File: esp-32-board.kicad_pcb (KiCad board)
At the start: 2 copper layers, 53.8 x 69.1 mm, 35 parts, among them J1 Conn_Arduino_UNO_R3, J2 Conn_02x03_Odd_Even, J3 ESP-PROG-Program, J4 ESP-PROG-Debug, J5 Barrel_Jack_MountingPin, J6 USB_B_Micro, Q2 ?, Q3 ?, SW1 SW_Push, SW2 SW_Push, SW3 SW_SPST, U1 ESP32-WROOM-32, U3 NCP1117-3.3, U4 NCP1117ST50T3G, U5 USBLC6-2SC6, U6 CP2102N-A01-GQFN28

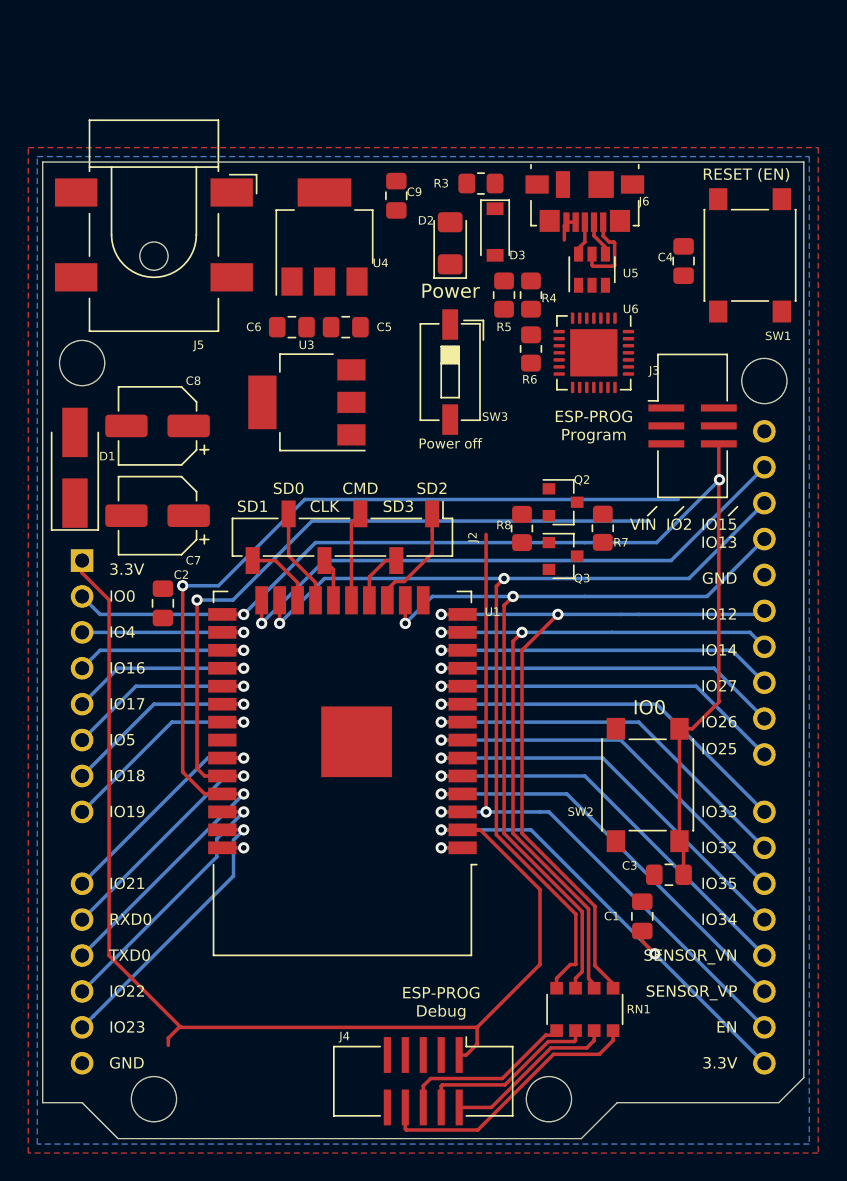
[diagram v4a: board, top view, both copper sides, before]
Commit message: Connect rest of tracks
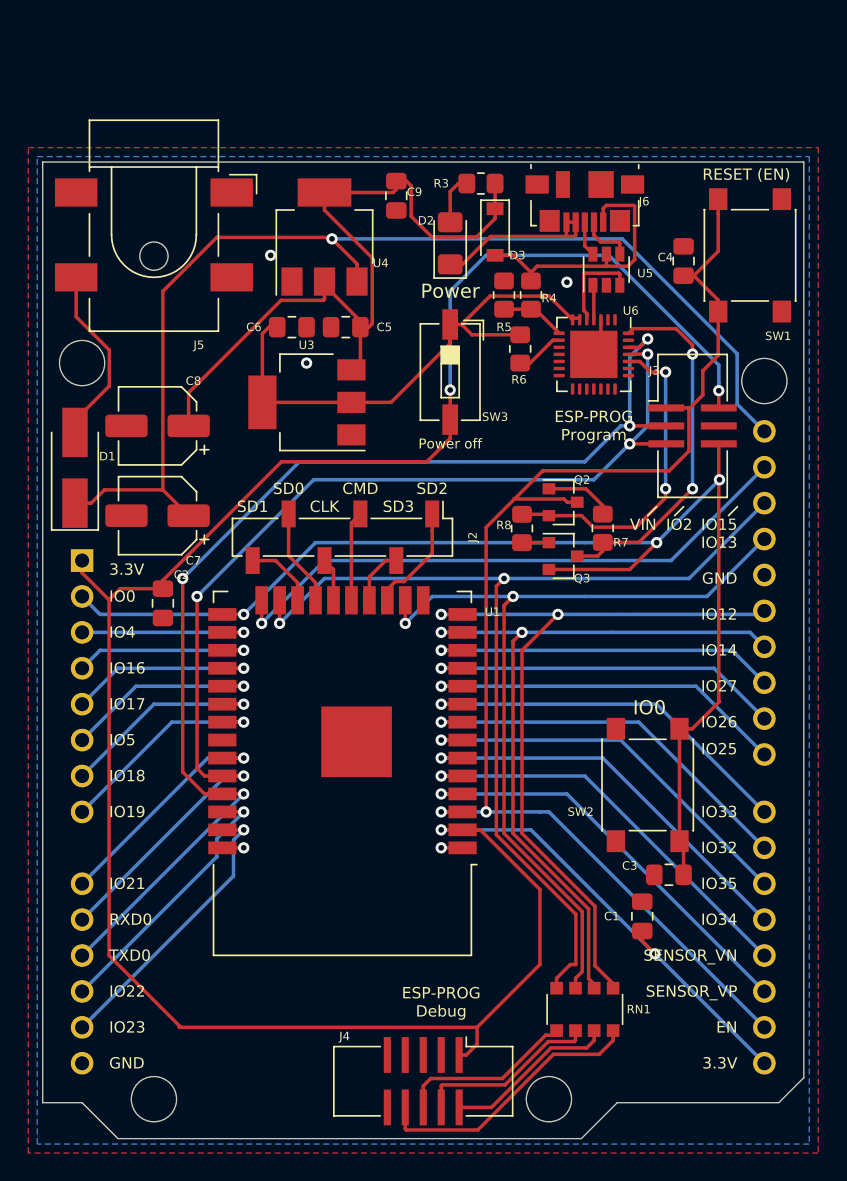
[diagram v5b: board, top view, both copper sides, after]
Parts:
- moved U5 1.02 mm to (169.2, 29.0)
- moved R6 0.76 mm to (163.1, 34.6)
- moved U6 0.11 mm to (168.3, 34.9)
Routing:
- net VDC: track 0.00 -> 78.9 mm, vias 0 -> 1
- net +3V3: track 113.4 -> 177.7 mm, vias 2 -> 4
- net +5V: track 0.00 -> 53.8 mm
- net /EN: track 50.3 -> 94.4 mm
- net /Power/Internal_3V3: track 0.00 -> 37.6 mm
- net /USB/DTR: track 0.00 -> 25.8 mm, vias 0 -> 2
- net /USB/RTS: track 0.00 -> 23.2 mm, vias 0 -> 2
- net /USB/VBUS: track 6.01 -> 19.3 mm
- net GND: track 5.18 -> 18.2 mm, vias 2 -> 5
- net Net-(D1-Pad2): track 0.00 -> 13.0 mm
- net /RXD0: track 65.4 -> 77.2 mm, vias 2 -> 4
- net /TXD0: track 71.9 -> 81.8 mm, vias 2 -> 4
- net /IO0: track 83.4 -> 91.8 mm, vias 2 -> 3
- net /USB/USB_DN: track 0.00 -> 6.71 mm
- net Net-(Q2-Pad1): track 0.00 -> 4.90 mm
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
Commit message: Update DC connector
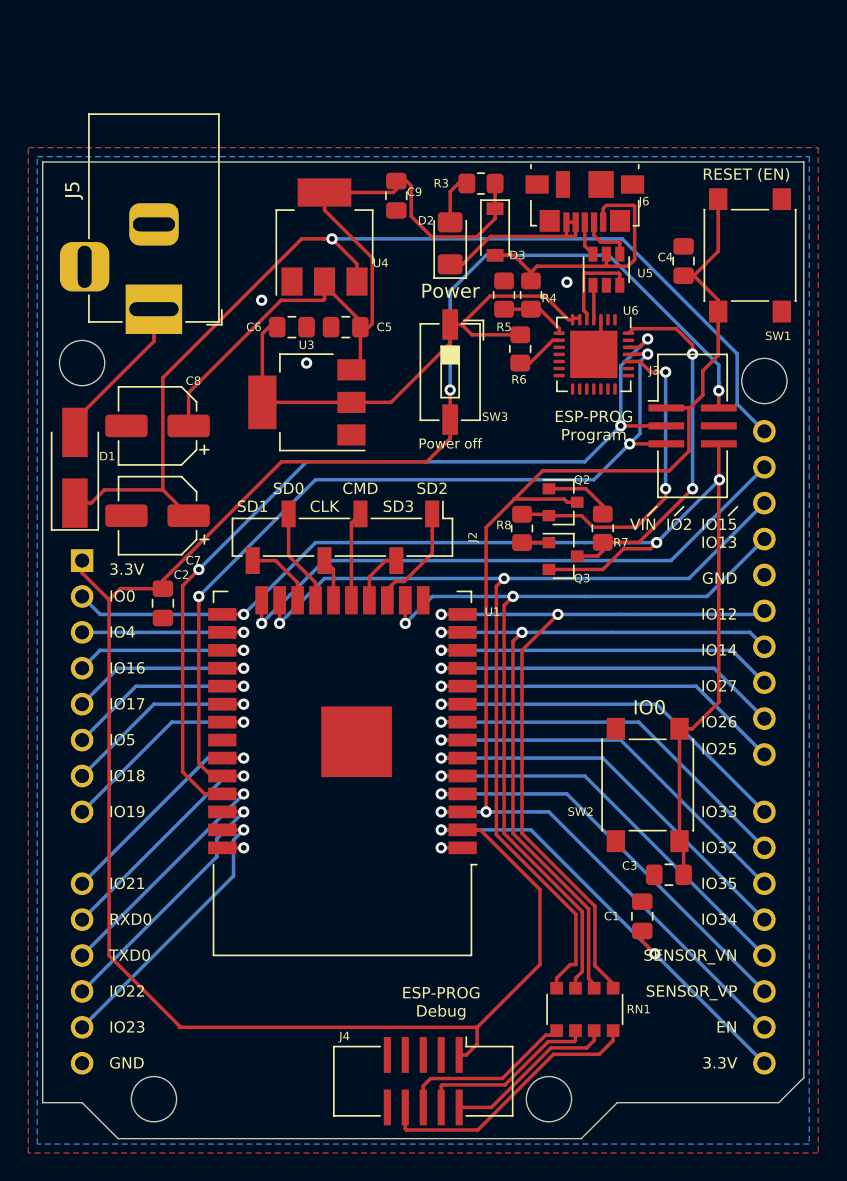
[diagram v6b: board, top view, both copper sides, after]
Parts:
- J5: footprint Connector_BarrelJack:BarrelJack_CLIFF_FC681465S_SMT_Horizontal -> Connector_BarrelJack:BarrelJack_Lumberg_1613-21_Horizontal
- moved J5 5.25 mm to (137.2, 31.8)
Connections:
- J5 pad 1: GND -> Net-(D1-Pad2)
- J5 pad 2: Net-(D1-Pad2) -> GND
- J5 pad 3: (no net) -> GND
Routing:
- net VDC: track 78.9 -> 75.2 mm
- net Net-(D1-Pad2): track 13.0 -> 11.0 mm

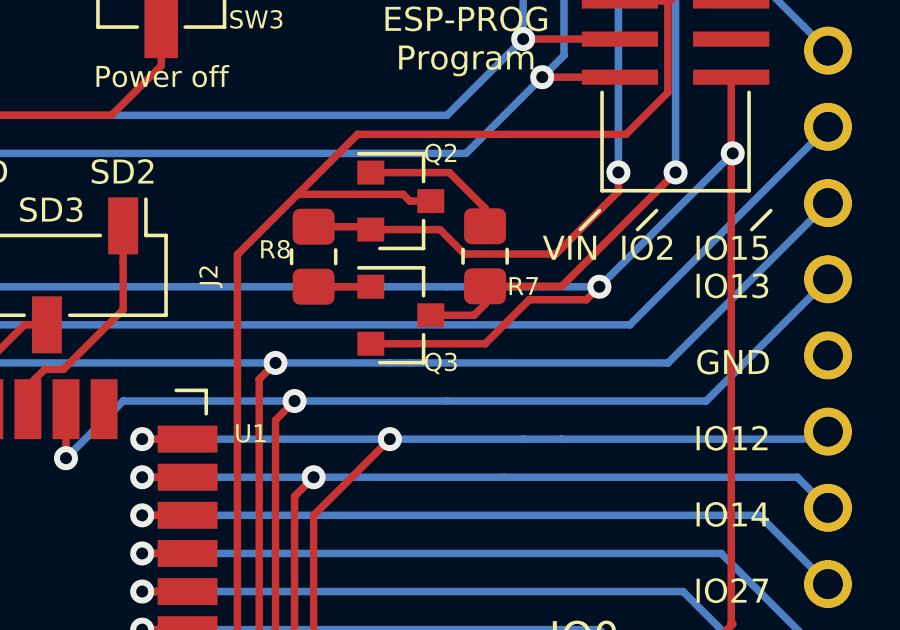
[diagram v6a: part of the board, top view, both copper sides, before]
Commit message: Fix auto-reset circuit for ESP32
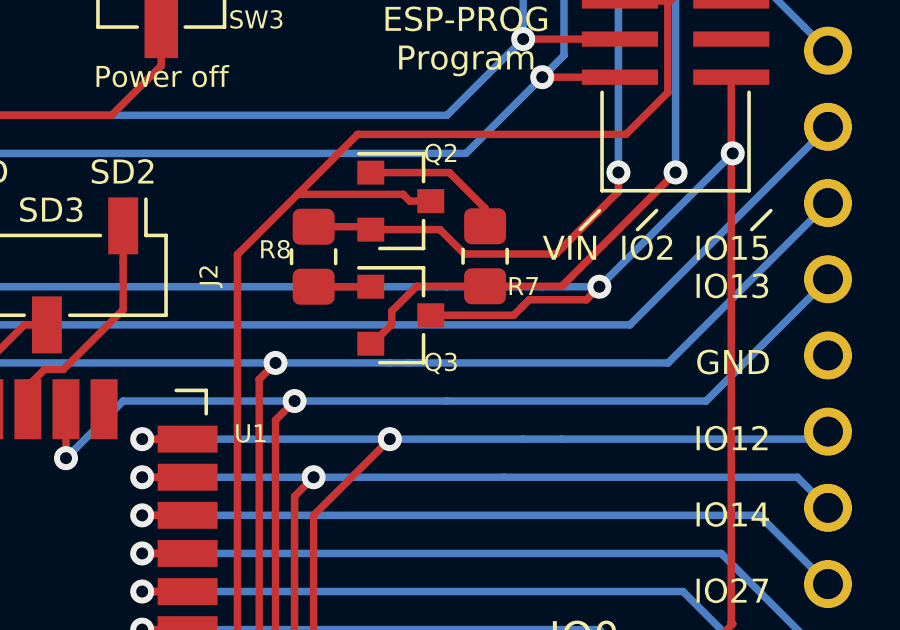
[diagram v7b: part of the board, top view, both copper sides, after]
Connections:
- Q3 pad 2: /IO0 -> /USB/DTR
- Q3 pad 3: /USB/DTR -> /IO0
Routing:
- net /IO0: track 91.8 -> 89.4 mm
- net /USB/DTR: track 25.8 -> 28.1 mm
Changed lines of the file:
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@@
     (thickness 1.6)
     (drawings 56)
-    (tracks 522)
+    (tracks 525)
     (zones 0)
     (modules 35)
@@
     )
     (pad 3 smd rect (at 1 0) (size 0.9 0.8) (layers F.Cu F.Paste F.Mask)
+      (net 4 /IO0))
+    (pad 2 smd rect (at -1 0.95) (size 0.9 0.8) (layers F.Cu F.Paste F.Mask)
       (net 43 /USB/DTR))
-    (pad 2 smd rect (at -1 0.95) (size 0.9 0.8) (layers F.Cu F.Paste F.Mask)
-      (net 4 /IO0))
     (pad 1 smd rect (at -1 -0.95) (size 0.9 0.8) (layers F.Cu F.Paste F.Mask)
       (net 39 "Net-(Q3-Pad1)"))
@@
   (segment (start 167.64 48.26) (end 170.815 48.26) (width 0.25) (layer B.Cu) (net 4))
   (segment (start 170.815 48.26) (end 172.72 48.26) (width 0.25) (layer B.Cu) (net 4))
-  (segment (start 165.1 50.16) (end 168.915 50.16) (width 0.25) (layer F.Cu) (net 4))
   (segment (start 170.38099 48.69401) (end 172.28599 48.69401) (width 0.25) (layer F.Cu) (net 4))
-  (segment (start 168.915 50.16) (end 170.38099 48.69401) (width 0.25) (layer F.Cu) (net 4))
   (segment (start 172.28599 48.69401) (end 172.72 48.26) (width 0.25) (layer F.Cu) (net 4))
   (segment (start 172.72 48.26) (end 172.72 48.26) (width 0.25) (layer F.Cu) (net 4))
   (via (at 172.72 48.26) (size 0.8) (drill 0.4) (layers F.Cu B.Cu) (net 4))
+  (segment (start 167.1 49.21) (end 169.865 49.21) (width 0.25) (layer F.Cu) (net 4))
+  (segment (start 169.865 49.21) (end 170.18 48.895) (width 0.25) (layer F.Cu) (net 4))
+  (segment (start 170.18 48.895) (end 170.38099 48.69401) (width 0.25) (layer F.Cu) (net 4))
   (segment (start 158.995 67.31) (end 157.48 67.31) (width 0.25) (layer F.Cu) (net 5))
   (segment (start 157.48 67.31) (end 157.48 67.31) (width 0.25) (layer F.Cu) (net 5))
@@
   (segment (start 173.355 44.45) (end 173.355 44.45) (width 0.25) (layer F.Cu) (net 42))
   (via (at 173.355 44.45) (size 0.8) (drill 0.4) (layers F.Cu B.Cu) (net 42))
-  (segment (start 168.91 48.844) (end 168.91 48.244) (width 0.25) (layer F.Cu) (net 43))
-  (segment (start 168.544 49.21) (end 168.91 48.844) (width 0.25) (layer F.Cu) (net 43))
-  (segment (start 167.1 49.21) (end 168.544 49.21) (width 0.25) (layer F.Cu) (net 43))
   (segment (start 171.046003 33.126997) (end 174.096997 33.126997) (width 0.25) (layer F.Cu) (net 43))
   (segment (start 170.725 33.448) (end 171.046003 33.126997) (width 0.25) (layer F.Cu) (net 43))
@@
   (via (at 175.26 34.925) (size 0.8) (drill 0.4) (layers F.Cu B.Cu) (net 43))
   (segment (start 175.26 34.925) (end 175.26 44.45) (width 0.25) (layer B.Cu) (net 43))
+  (segment (start 165.15 50.16) (end 165.1 50.16) (width 0.25) (layer F.Cu) (net 43))
+  (segment (start 165.8 49.074998) (end 165.8 49.51) (width 0.25) (layer F.Cu) (net 43))
+  (segment (start 166.630998 48.244) (end 165.8 49.074998) (width 0.25) (layer F.Cu) (net 43))
+  (segment (start 165.8 49.51) (end 165.15 50.16) (width 0.25) (layer F.Cu) (net 43))
+  (segment (start 168.91 48.244) (end 166.630998 48.244) (width 0.25) (layer F.Cu) (net 43))
   (segment (start 137.16 33.75) (end 137.16 31.75) (width 0.25) (layer F.Cu) (net 44))
   (segment (start 137.16 34.028) (end 137.16 33.75) (width 0.25) (layer F.Cu) (net 44))

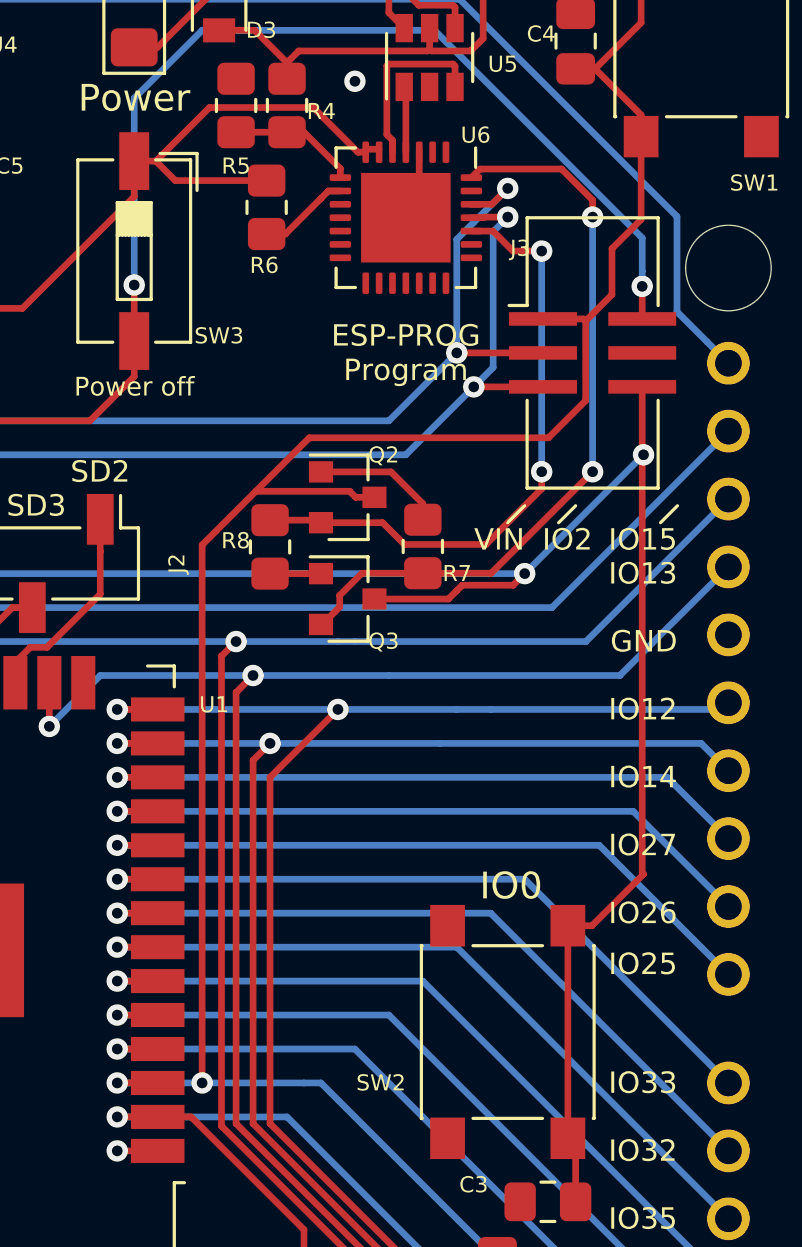
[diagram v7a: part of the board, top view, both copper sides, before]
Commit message: Replace auto-reset circuit with single BCR129S chip
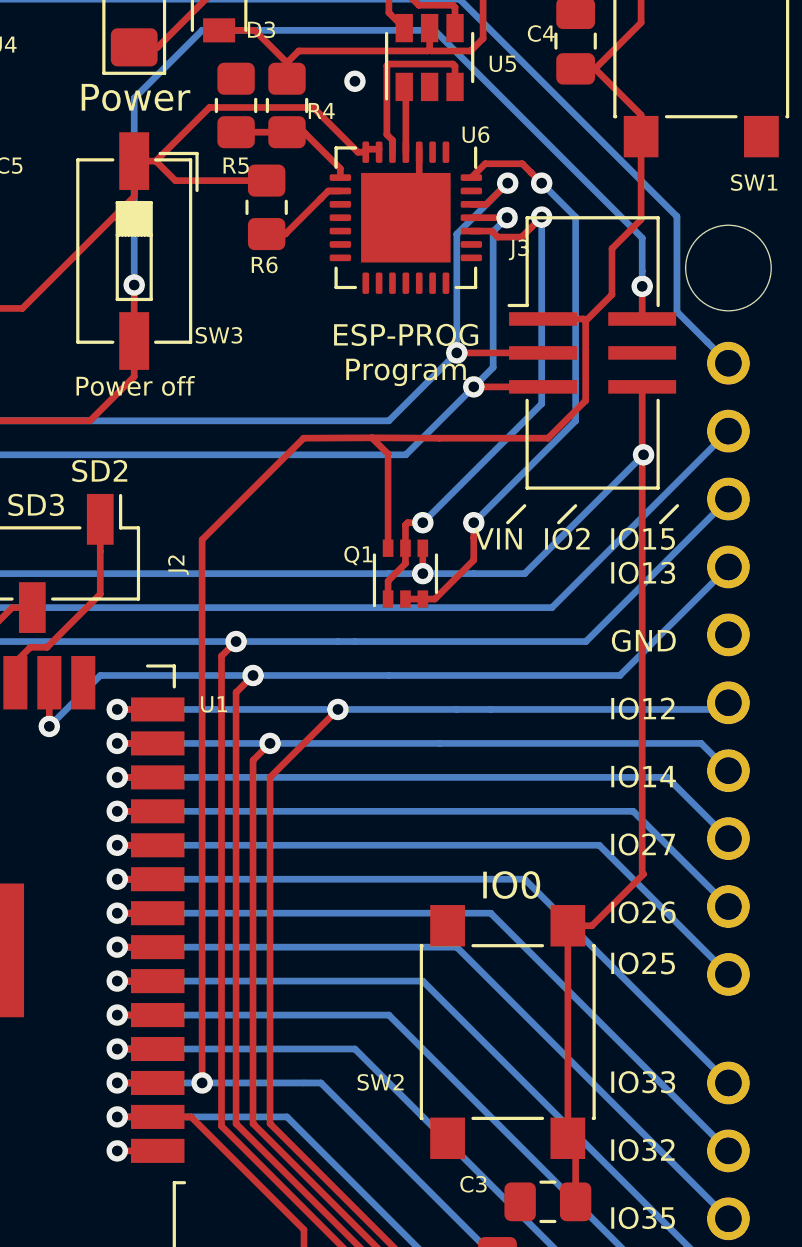
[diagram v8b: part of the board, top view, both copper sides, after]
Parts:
- removed Q2, Q3: ?, Package_TO_SOT_SMD:SOT-23
- removed R7, R8: 10k Ohm, Resistor_SMD:R_0805_2012Metric_Pad1.20x1.40mm_HandSolder
- added Q1: BCR129S, Package_TO_SOT_SMD:SOT-363_SC-70-6, F.Cu at (168.3, 48.3)
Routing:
- net /USB/DTR: track 28.1 -> 22.5 mm
- net /IO0: track 89.4 -> 84.3 mm
- net Net-(Q2-Pad1): track 4.90 -> 0.00 mm
- net /USB/RTS: track 23.2 -> 20.0 mm
- net Net-(Q3-Pad1): track 1.91 -> 0.00 mm
